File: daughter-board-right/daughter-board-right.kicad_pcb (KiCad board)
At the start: 2 copper layers, 40 x 30 mm, 20 parts, among them J1 Conn_01x06_MountingPin, J2 USB_C_Receptacle_USB2.0_16P, J3 PJ-320A, U1 SRV05-4

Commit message: quick save
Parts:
- J1: footprint Connector_JST:JST_SHL_SM06B-SHLS-TF_1x06-1MP_P1.00mm_Horizontal -> Connector_JST:JST_SH_SM06B-SRSS-TB_1x06-1MP_P1.00mm_Horizontal
- moved C4 6.00 mm to (105.2, 75.5)
- moved C5 6.00 mm to (137.2, 75.5)
- moved H3 6.00 mm to (104.0, 80.0)
- moved H4 6.00 mm to (136.0, 80.0)
- moved R6 6.00 mm to (102.8, 75.5)
- moved R7 6.00 mm to (134.8, 75.5)
- moved J1 5.50 mm to (120.0, 80.0)
- moved R2 1.66 mm to (133.9, 72.2), turned to 0 degrees
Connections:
- net Net-(J2-SHIELD) renamed /SHIELD
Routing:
- net /SPLIT_TX: track 19.4 -> 13.9 mm
- net /SPLIT_RX: track 23.0 -> 17.5 mm
- net +5V: track 52.4 -> 48.2 mm
- net /USB_D-: track 24.8 -> 22.8 mm
- net /USB_D+: track 24.7 -> 22.8 mm
- net Net-(J2-CC1): track 8.68 -> 8.03 mm
- net GND: vias 37 -> 28
- net /SHIELD: vias 1 -> 0
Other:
- board size 40 x 30 mm -> 40 x 24 mm

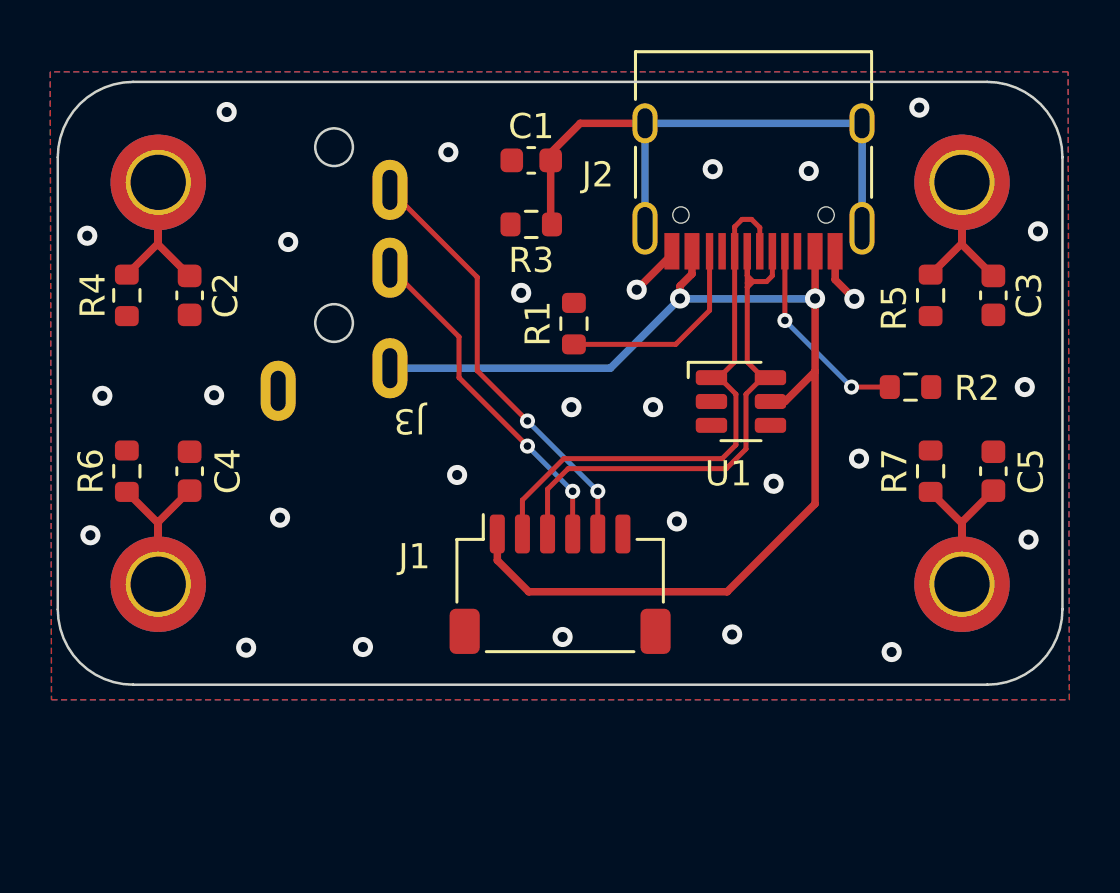
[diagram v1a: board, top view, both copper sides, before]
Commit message: finalised first version of pcbs for prototype order added openscad file for the left halfs case
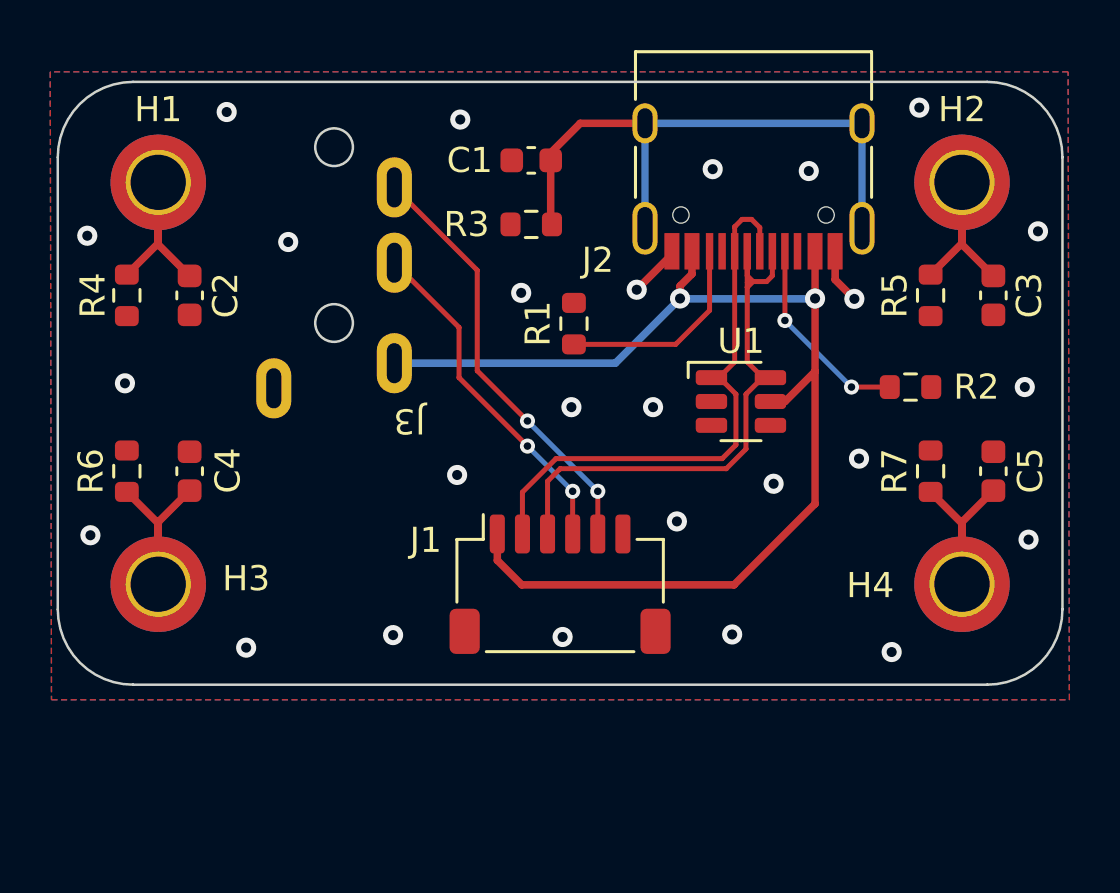
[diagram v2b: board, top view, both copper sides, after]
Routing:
- net GND: vias 28 -> 26
